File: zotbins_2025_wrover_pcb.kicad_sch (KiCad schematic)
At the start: 45 parts, among them J1 FFC2B28-24-G, J2 DCJ200-10-A-XX-K_REVA, J3 HC-SR04_Screw_Terminal_01x04, J4 HX711_Screw_Terminal_01x05, J5 Main_Servo_Screw_Terminal_01x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, J6 Conn_01x30_Pin, J7 SG_Servo_Screw_Terminal_01x03, J8 BB_Receiver_Screw_Terminal_01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, J9 BB_Transmitter_Screw_Terminal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, Q1 IRLML9301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

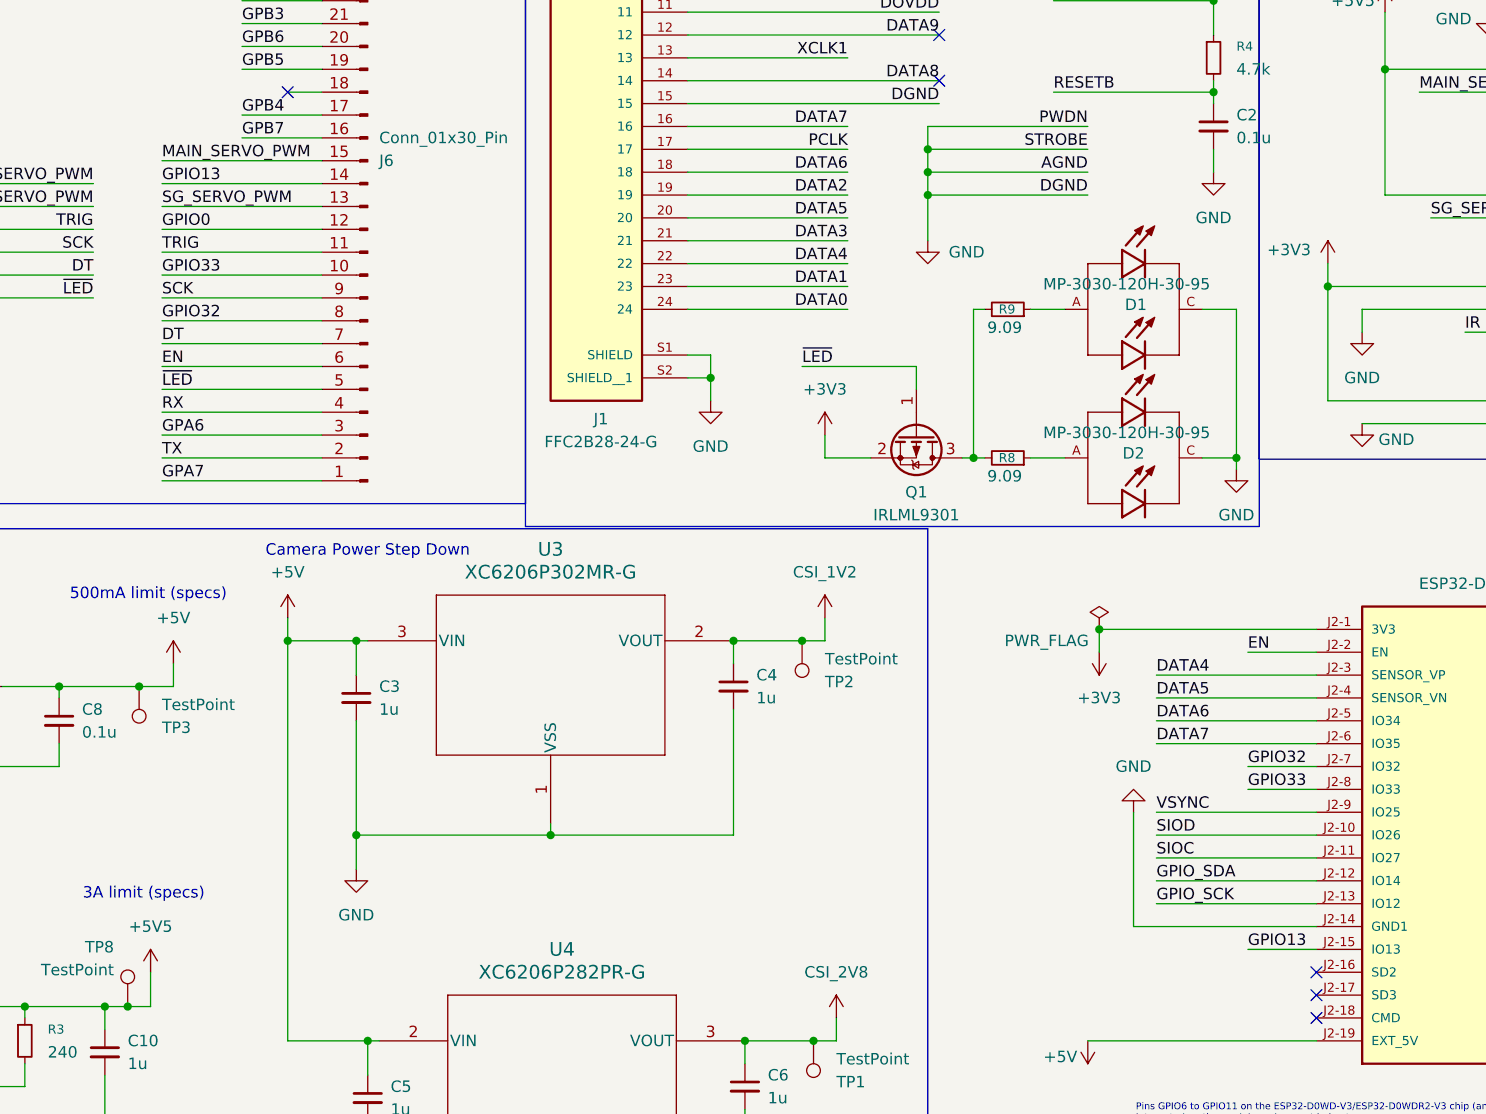
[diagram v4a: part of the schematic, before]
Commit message: fixed GPIO issue within gpio expander
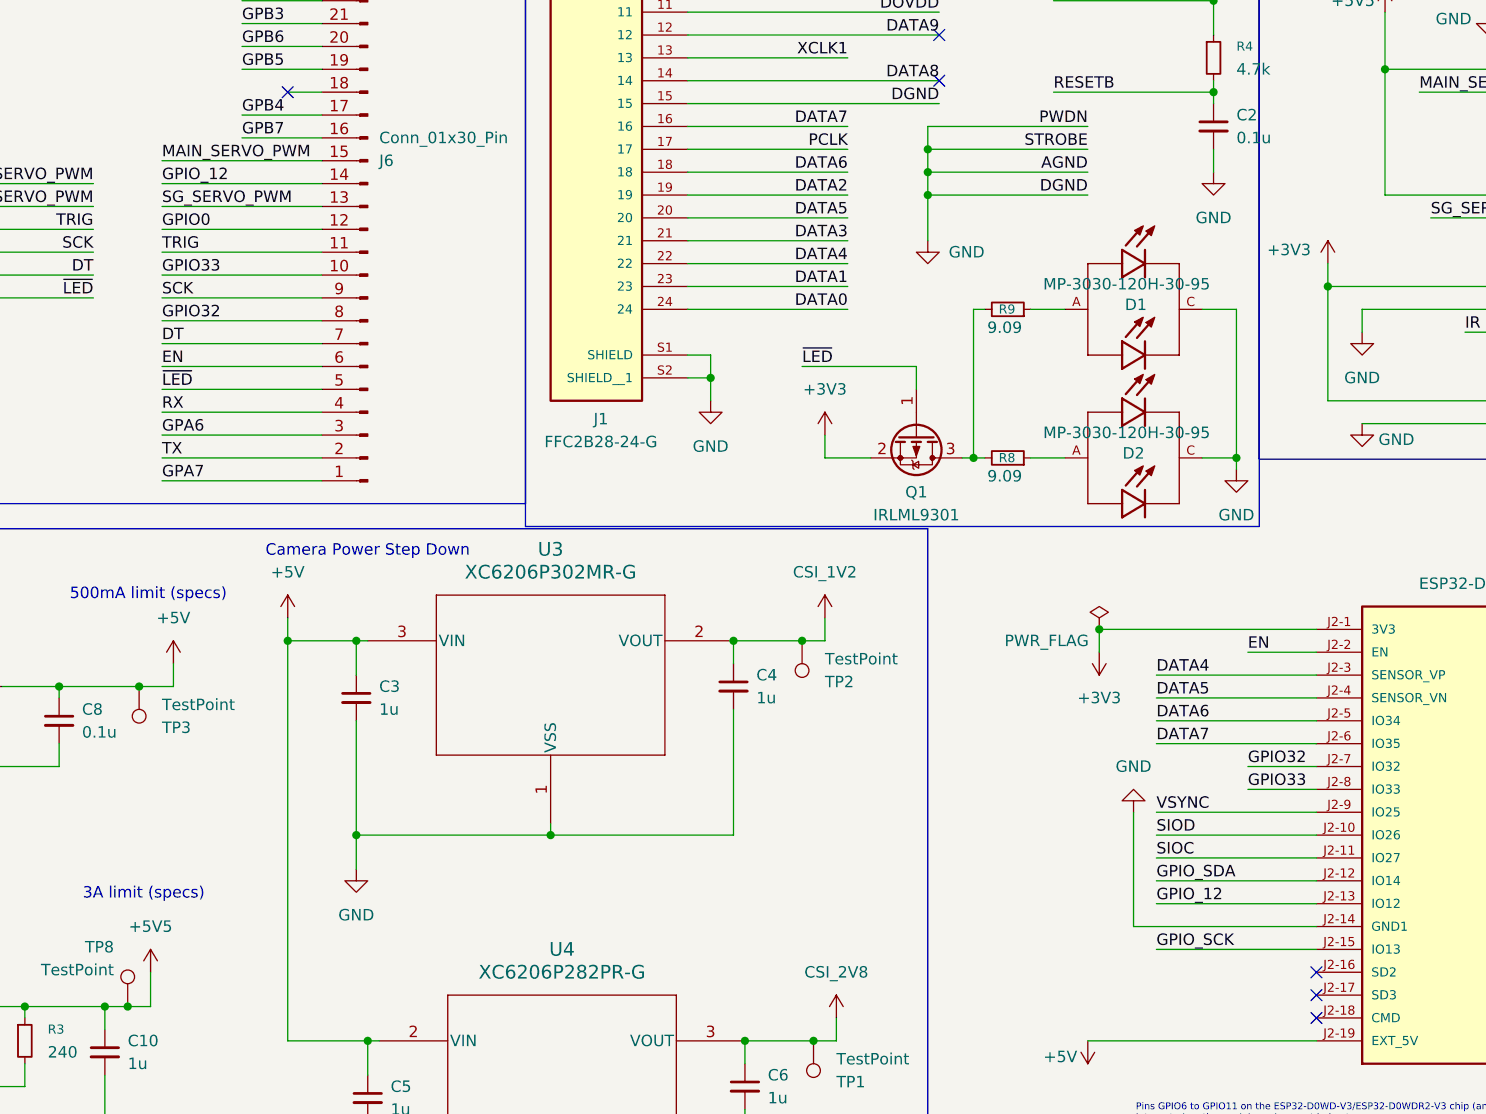
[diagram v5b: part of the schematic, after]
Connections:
- net GPIO_SCK: now also U6.J2-15 (IO13); no longer U6.J2-13 (IO12)
- net GPIO13 renamed GPIO_12
- net GPIO_12: now also U6.J2-13 (IO12); no longer U6.J2-15 (IO13)
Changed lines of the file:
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@@
 	(wire
 		(pts
+			(xy 90.17 66.04) (xy 107.95 66.04)
+		)
+		(stroke
+			(width 0)
+			(type default)
+		)
+	)
+	(wire
+		(pts
 			(xy 81.28 38.1) (xy 107.95 38.1)
 		)
@@
 	(wire
 		(pts
+			(xy 200.66 146.05) (xy 218.44 146.05)
+		)
+		(stroke
+			(width 0)
+			(type default)
+		)
+	)
+	(wire
+		(pts
 			(xy 90.17 96.52) (xy 107.95 96.52)
 		)
@@
 	(wire
 		(pts
-			(xy 200.66 146.05) (xy 218.44 146.05)
-		)
-		(stroke
-			(width 0)
-			(type default)
-		)
-	)
-	(wire
-		(pts
 			(xy 111.76 116.84) (xy 111.76 120.65)
 		)
@@
 	(wire
 		(pts
-			(xy 90.17 66.04) (xy 107.95 66.04)
+			(xy 107.95 30.48) (xy 105.41 30.48)
 		)
 		(stroke
@@
 	(wire
 		(pts
-			(xy 107.95 30.48) (xy 105.41 30.48)
+			(xy 276.86 146.05) (xy 259.08 146.05)
 		)
 		(stroke
@@
 	(wire
 		(pts
-			(xy 276.86 146.05) (xy 259.08 146.05)
+			(xy 25.4 81.28) (xy 27.94 81.28)
 		)
 		(stroke
@@
 	(wire
 		(pts
-			(xy 25.4 81.28) (xy 27.94 81.28)
+			(xy 241.3 46.99) (xy 241.3 50.8)
 		)
 		(stroke
@@
 	(wire
 		(pts
-			(xy 241.3 46.99) (xy 241.3 50.8)
+			(xy 105.41 22.86) (xy 105.41 25.4)
 		)
 		(stroke
@@
 	(wire
 		(pts
-			(xy 105.41 22.86) (xy 105.41 25.4)
+			(xy 200.66 151.13) (xy 218.44 151.13)
 		)
 		(stroke
@@
 	(wire
 		(pts
-			(xy 210.82 151.13) (xy 218.44 151.13)
-		)
-		(stroke
-			(width 0)
-			(type default)
-		)
-	)
-	(wire
-		(pts
 			(xy 166.37 41.91) (xy 148.59 41.91)
 		)
@@
 		)
 	)
+	(label "GPIO_12"
+		(at 200.66 146.05 0)
+		(effects
+			(font
+				(size 1.27 1.27)
+			)
+			(justify left bottom)
+		)
+	)
 	(label "TRIG"
 		(at 90.17 73.66 0)
@@
 		)
 	)
-	(label "GPIO_SCK"
-		(at 200.66 146.05 0)
-		(effects
-			(font
-				(size 1.27 1.27)
-			)
-			(justify left bottom)
-		)
-	)
 	(label "ECHO"
 		(at 69.85 43.18 180)
@@
 		)
 	)
-	(label "GPIO13"
-		(at 90.17 66.04 0)
-		(effects
-			(font
-				(size 1.27 1.27)
-			)
-			(justify left bottom)
-		)
-	)
 	(label "DT"
 		(at 82.55 76.2 180)
@@
 		)
 	)
-	(label "GPIO13"
-		(at 210.82 151.13 0)
-		(effects
-			(font
-				(size 1.27 1.27)
-			)
-			(justify left bottom)
-		)
-	)
 	(label "RX"
 		(at 90.17 91.44 0)
@@
 		(effects
 			(font
+				(size 1.27 1.27)
+			)
+			(justify left bottom)
+		)
+	)
+	(label "GPIO_12"
+		(at 90.17 66.04 0)
+		(effects
+			(font
+				(size 1.27 1.27)
+			)
+			(justify left bottom)
+		)
+	)
+	(label "GPIO_SCK"
+		(at 200.66 151.13 0)
+		(effects
+			(font

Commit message: iteration 2 modified, components changed
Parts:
- removed D1, D2: MP-3030-120H-30-95, LED:LED_MP-3030-120H-30-95, symbol LED-Flash:MP-3030-120H-30-95
- removed J1: FFC2B28-24-G, Library:GCT_FFC2B28-24-G, symbol Connector:FFC2B28-24-G
- removed Q1: IRLML9301, Package_TO_SOT_SMD:SOT-23, symbol Transistor_FET:IRLML9301
- removed R8, R9: 9.09, Resistor_THT:R_Axial_DIN0207_L6.3mm_D2.5mm_P10.16mm_Horizontal, symbol Device:R_Small
- added J1: Conn_01x28_Pin, Connector_FFC-FPC:TE_2-84953-8_1x28-1MP_P1.0mm_Horizontal, symbol Connector:Conn_01x28_Pin
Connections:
- net +3V3: now also J1.11 (Pin_11), J1.26 (Pin_26)
- net CSI_1V2: now also J1.10 (Pin_10)
- net CSI_2V8: now also J1.4 (Pin_4)
- net DATA0: now also J1.24 (Pin_24)
- net DATA1: now also J1.23 (Pin_23)
- net DATA2: now also J1.19 (Pin_19)
- net DATA3: now also J1.21 (Pin_21)
- net DATA4: now also J1.22 (Pin_22)
- net DATA5: now also J1.20 (Pin_20)
- net DATA6: now also J1.18 (Pin_18)
- net DATA7: now also J1.16 (Pin_16)
- net DATA8: now also J1.14 (Pin_14)
- net DATA9: now also J1.12 (Pin_12)
- net GND: now also J1.27 (Pin_27), J1.28 (Pin_28)
- net HREF: now also J1.9 (Pin_9)
- net PCLK: now also J1.17 (Pin_17)
- net RESETB: now also J1.6 (Pin_6)
- net SIOC: now also J1.5 (Pin_5)
- net SIOD: now also J1.3 (Pin_3)
- net VSYNC: now also J1.7 (Pin_7)
- net XCLK1: now also J1.13 (Pin_13)
- net ~{LED}: now also J1.25 (Pin_25)
- new net AGND: J1.2 (Pin_2)
- new net DGND: J1.15 (Pin_15)
- new net PWDN: J1.8 (Pin_8)
- new net STROBE: J1.1 (Pin_1)
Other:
- note added: "The camera pins are connected via a flat-ribbon cable to an external camera PCB. PDWN, STROBE, AGND, DGND are connected to GND on the Camera PCB"
- moved on the sheet: C2, R4, TP6

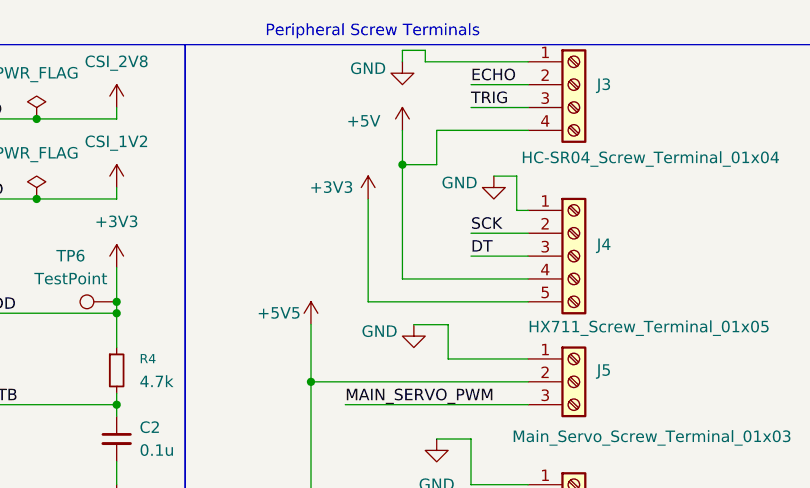
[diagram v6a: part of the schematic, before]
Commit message: changed hcsr04 power to 3V3 as this component changed models
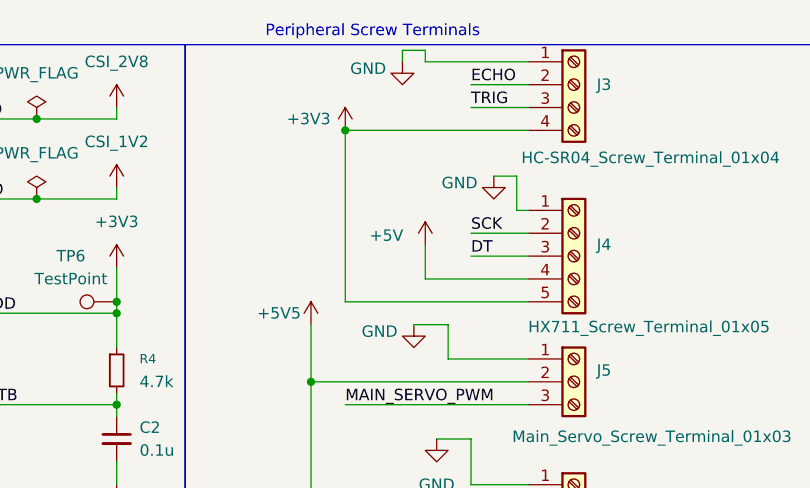
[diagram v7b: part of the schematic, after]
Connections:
- net +3V3: now also J3.4 (Pin_4)
- net +5V: no longer J3.4 (Pin_4)
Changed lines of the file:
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@@
 	)
 	(junction
-		(at 236.22 29.21)
-		(diameter 0)
-		(color 0 0 0 0)
-	)
-	(junction
 		(at 194.31 115.57)
 		(diameter 0)
@@
 	)
 	(junction
+		(at 229.87 25.4)
+		(diameter 0)
+		(color 0 0 0 0)
+	)
+	(junction
 		(at 25.4 81.28)
 		(diameter 0)
@@
 	(wire
 		(pts
-			(xy 240.03 25.4) (xy 250.19 25.4)
-		)
-		(stroke
-			(width 0)
-			(type default)
-		)
-	)
-	(wire
-		(pts
 			(xy 166.37 69.85) (xy 148.59 69.85)
 		)
@@
 	(wire
 		(pts
-			(xy 236.22 29.21) (xy 236.22 41.91)
-		)
-		(stroke
-			(width 0)
-			(type default)
-		)
-	)
-	(wire
-		(pts
 			(xy 153.67 116.84) (xy 161.29 116.84)
 		)
@@
 	(wire
 		(pts
-			(xy 236.22 25.4) (xy 236.22 29.21)
+			(xy 238.76 38.1) (xy 238.76 41.91)
 		)
 		(stroke
@@
 	(wire
 		(pts
-			(xy 250.19 44.45) (xy 232.41 44.45)
+			(xy 250.19 44.45) (xy 229.87 44.45)
 		)
 		(stroke
@@
 	(wire
 		(pts
-			(xy 232.41 33.02) (xy 232.41 44.45)
+			(xy 229.87 25.4) (xy 229.87 44.45)
 		)
 		(stroke
@@
 	(wire
 		(pts
-			(xy 250.19 41.91) (xy 236.22 41.91)
+			(xy 250.19 41.91) (xy 238.76 41.91)
 		)
 		(stroke
@@
 	(wire
 		(pts
-			(xy 240.03 29.21) (xy 240.03 25.4)
-		)
-		(stroke
-			(width 0)
-			(type default)
-		)
-	)
-	(wire
-		(pts
 			(xy 81.28 35.56) (xy 107.95 35.56)
 		)
@@
 	(wire
 		(pts
+			(xy 229.87 25.4) (xy 250.19 25.4)
+		)
+		(stroke
+			(width 0)
+			(type default)
+		)
+	)
+	(wire
+		(pts
 			(xy 204.47 62.23) (xy 204.47 64.77)
 		)
@@
 	(wire
 		(pts
-			(xy 236.22 29.21) (xy 240.03 29.21)
-		)
-		(stroke
-			(width 0)
-			(type default)
-		)
-	)
-	(wire
-		(pts
 			(xy 243.84 36.83) (xy 250.19 36.83)
 		)
@@
 	(symbol
 		(lib_id "power:+5V")
-		(at 236.22 25.4 0)
+		(at 238.76 38.1 0)
 		(unit 1)
 		(exclude_from_sim no)
@@
 		(dnp no)
 		(property "Reference" "#PWR019"
-			(at 236.22 29.21 0)
+			(at 238.76 41.91 0)
 			(effects
 				(font
@@
 		)
 		(property "Value" "+5V"
-			(at 231.902 24.384 0)
+			(at 234.442 37.084 0)
 			(effects
 				(font
@@
 		)
 		(property "Footprint" ""
-			(at 236.22 25.4 0)
+			(at 238.76 38.1 0)
 			(effects
 				(font
@@
 		)
 		(property "Datasheet" ""
-			(at 236.22 25.4 0)
+			(at 238.76 38.1 0)
 			(effects
 				(font
@@
 		)
 		(property "Description" "Power symbol creates a global label with name \"+5V\""
-			(at 236.22 25.4 0)
+			(at 238.76 38.1 0)
 			(effects
 				(font
@@
 	(symbol
 		(lib_id "power:+3V3")
-		(at 232.41 33.02 0)
+		(at 229.87 25.4 0)
 		(mirror y)
 		(unit 1)
@@
 		(dnp no)
 		(property "Reference" "#PWR034"
-			(at 232.41 36.83 0)
+			(at 229.87 29.21 0)
 			(effects
 				(font
@@
 		)
 		(property "Value" "+3V3"
-			(at 228.346 31.75 0)
+			(at 225.806 24.13 0)
 			(effects
 				(font
@@
 		)
 		(property "Footprint" ""
-			(at 232.41 33.02 0)
+			(at 229.87 25.4 0)
 			(effects
 				(font
@@
 		)
 		(property "Datasheet" ""
-			(at 232.41 33.02 0)
+			(at 229.87 25.4 0)
 			(effects
 				(font
@@
 		)
 		(property "Description" "Power symbol creates a global label with name \"+3V3\""
-			(at 232.41 33.02 0)
+			(at 229.87 25.4 0)
 			(effects
 				(font
